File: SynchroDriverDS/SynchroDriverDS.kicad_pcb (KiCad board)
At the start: 2 copper layers, 67 x 33 mm, 46 parts, among them J1 POWER, J2 CTRL, J3 Conn_01x04, Q1 2N7002, Q2 2N7002, Q3 2N7002, Q4 SIS990, Q5 SIS990, Q6 SIS990, U1 DRV8300

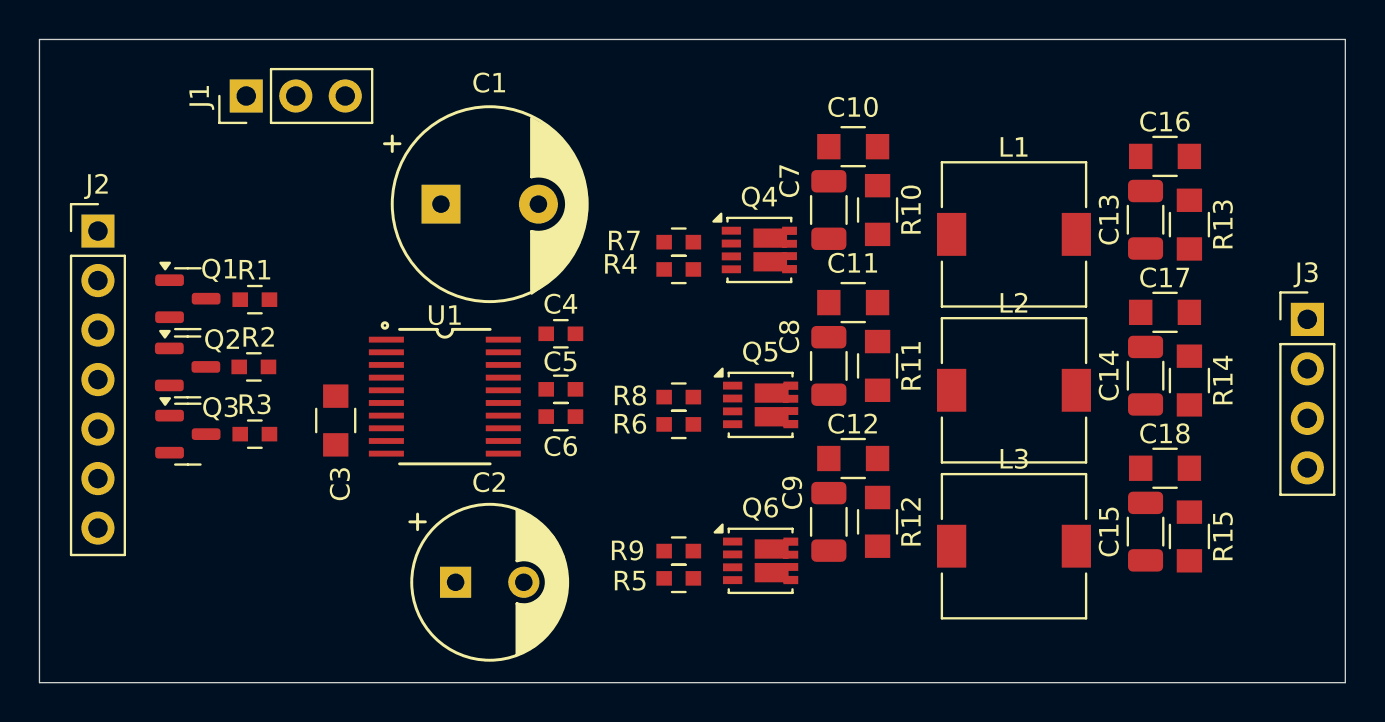
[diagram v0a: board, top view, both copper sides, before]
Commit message: Update digital single synchro pcb
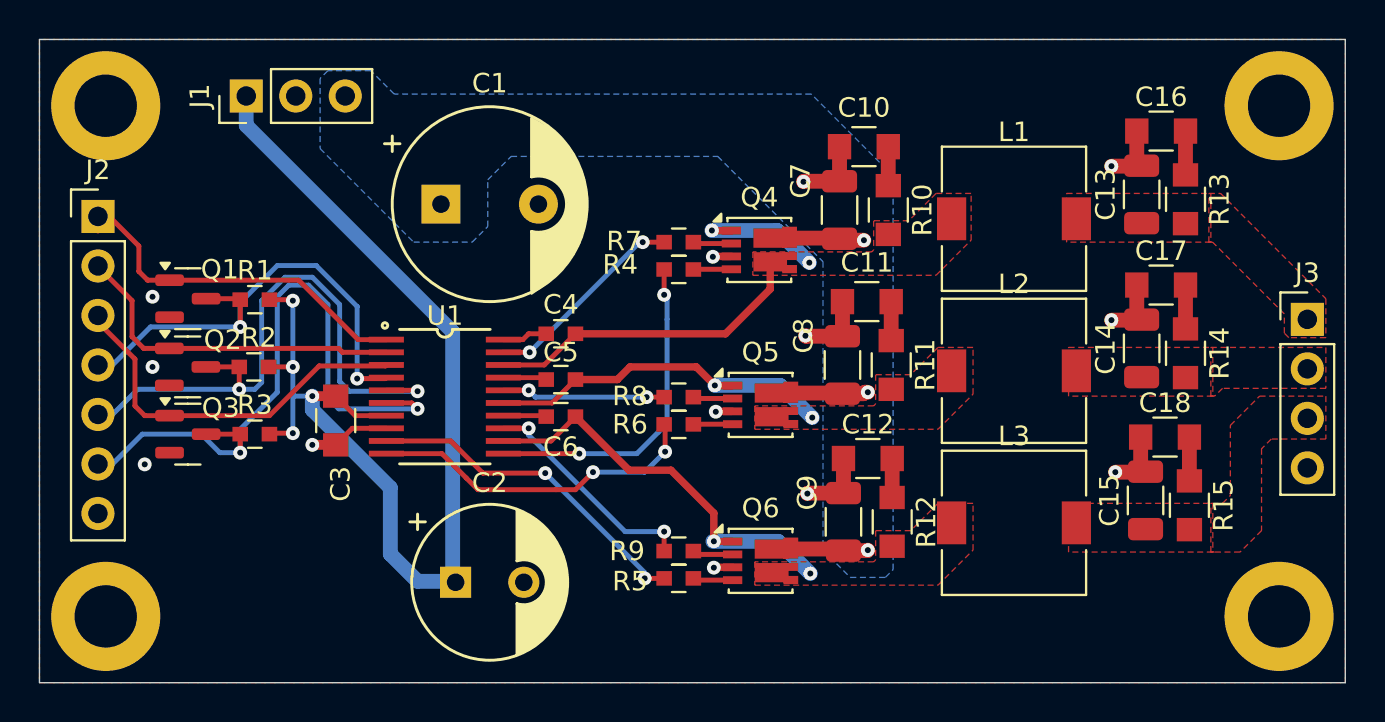
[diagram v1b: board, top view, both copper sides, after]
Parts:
- added H1: MountingHole_Pad, MountingHole:MountingHole_3.2mm_M3_DIN965_Pad, F.Cu at (123.4, 83.4)
- added H2: MountingHole_Pad, MountingHole:MountingHole_3.2mm_M3_DIN965_Pad, F.Cu at (123.4, 109.6)
- added H3: MountingHole_Pad, MountingHole:MountingHole_3.2mm_M3_DIN965_Pad, F.Cu at (183.6, 83.4)
- added H4: MountingHole_Pad, MountingHole:MountingHole_3.2mm_M3_DIN965_Pad, F.Cu at (183.6, 109.6)
- moved C15 1.60 mm to (176.8, 103.7)
- moved C18 1.60 mm to (177.8, 100.4)
- moved R15 1.60 mm to (179.0, 103.9)
- moved C14 1.41 mm to (176.6, 95.8)
- moved C17 1.41 mm to (177.6, 92.6)
- moved R14 1.41 mm to (178.8, 96.1)
- moved C13 1.32 mm to (176.6, 88.0)
- moved C16 1.32 mm to (177.6, 84.7)
- moved R13 1.32 mm to (178.8, 88.2)
- moved L3 1.20 mm to (170.0, 104.8)
- moved L2 1.00 mm to (170.0, 97.0)
- moved L1 0.80 mm to (170.0, 89.2)
- moved C12 0.75 mm to (162.5, 101.5)
- moved C9 0.75 mm to (161.2, 104.8)
- moved J2 0.75 mm to (123.0, 89.1)
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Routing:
- net +12V: track 0.00 -> 58.9 mm, vias 0 -> 4
- net /SingleSynchroDriver/INCL: track 0.00 -> 34.4 mm, vias 0 -> 2
- net /SingleSynchroDriver/INBL: track 0.00 -> 31.0 mm, vias 0 -> 2
- net GND: track 0.00 -> 28.2 mm, vias 0 -> 13
- net /SingleSynchroDriver/INAL: track 0.00 -> 25.4 mm, vias 0 -> 2
- net Net-(Q4A-S): track 0.00 -> 23.4 mm, vias 0 -> 2
- net Net-(Q6A-S): track 0.00 -> 21.5 mm, vias 0 -> 2
- net /SingleSynchroDriver/INC: track 0.00 -> 19.6 mm
- net Net-(Q5A-S): track 0.00 -> 18.6 mm, vias 0 -> 2
- net /SingleSynchroDriver/INA: track 0.00 -> 18.4 mm
- net /SingleSynchroDriver/INB: track 0.00 -> 17.7 mm
- net Net-(U1-GLC): track 0.00 -> 17.3 mm, vias 0 -> 2
- net Net-(U1-GLB): track 0.00 -> 17.3 mm, vias 0 -> 2
- net Net-(U1-GLA): track 0.00 -> 17.0 mm, vias 0 -> 2
- net +36V: track 0.00 -> 14.8 mm, vias 0 -> 3
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- added copper zone on B.Cu, net +36V
- added copper zone on F.Cu, net /SingleSynchroDriver/PHASE_A_OUT
- added copper zone on F.Cu, net /SingleSynchroDriver/PHASE_B_OUT
- added copper zone on F.Cu, net /SingleSynchroDriver/PHASE_C_OUT
- added copper zone on B.Cu, net GND
- added copper zone on F.Cu, net GND
- added copper zone on F.Cu, net Net-(Q4A-S)
- added copper zone on F.Cu, net Net-(Q5A-S)
- added copper zone on F.Cu, net Net-(Q6A-S)

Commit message: Improve ref in, clearance for 115V
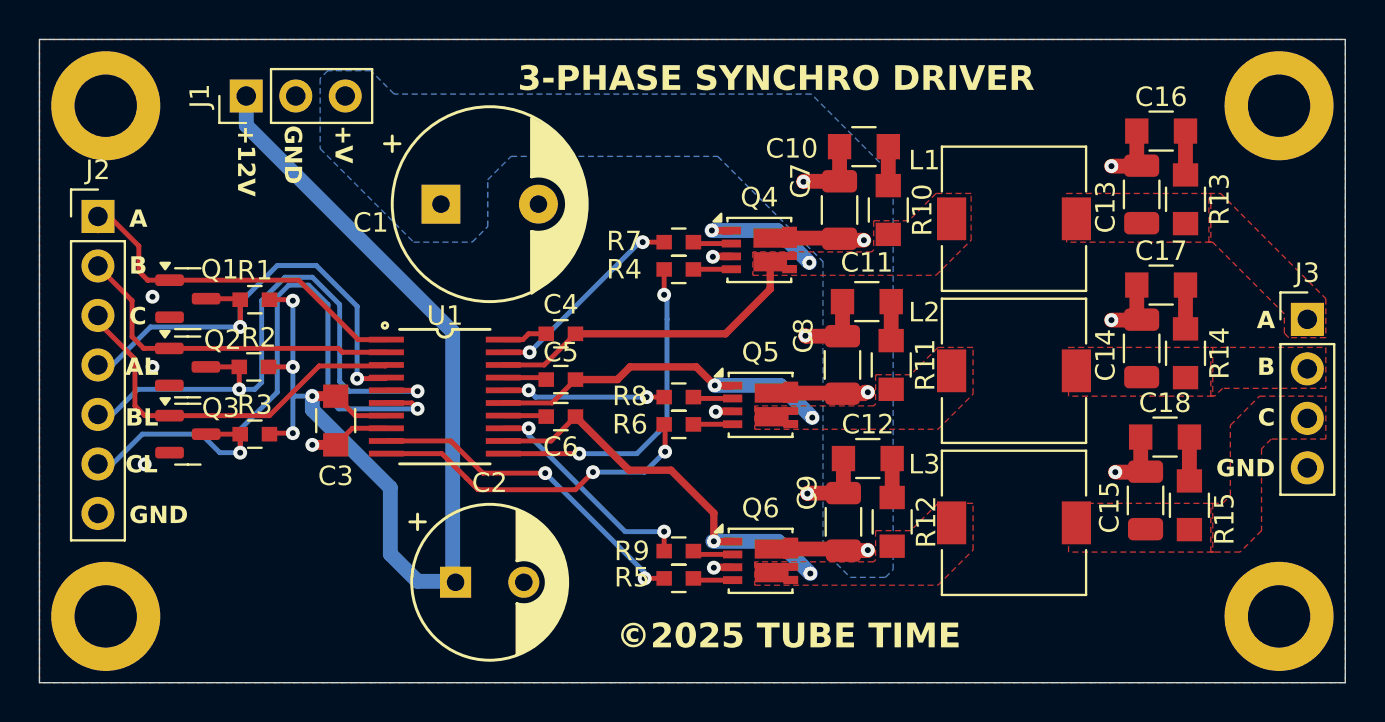
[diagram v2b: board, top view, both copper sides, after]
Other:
- board text added: "+12V"
- board text added: "+V"
- board text added: "3-PHASE SYNCHRO DRIVER"
- board text added: "A"
- board text added: "AL"
- board text added: "B"
- board text added: "BL"
- board text added: "C"
- board text added: "CL"
- board text added: "GND"
- board text added: "©2025 TUBE TIME"
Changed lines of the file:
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@@
 		(tags "resistor 0805")
 		(property "Reference" "C10"
-			(at 0 2 0)
+			(at 3.7 -0.1 0)
 			(layer "F.SilkS")
 			(effects
@@
 		(tags "Choke SMD")
 		(property "Reference" "L1"
-			(at 0 -4.45 0)
+			(at -4.6 -3 0)
 			(layer "F.SilkS")
 			(effects
@@
 		(tags "capacitor 0603")
 		(property "Reference" "R4"
-			(at -3 -0.25 0)
+			(at -2.8 0 0)
 			(layer "F.SilkS")
 			(effects
@@
 		(tags "capacitor")
 		(property "Reference" "C15"
-			(at 0 -1.85 90)
+			(at -0.35 -1.85 90)
 			(layer "F.SilkS")
 			(effects
@@
 		(tags "resistor 0805")
 		(property "Reference" "R15"
-			(at 0 1.75 90)
+			(at -0.7 1.8 90)
 			(layer "F.SilkS")
 			(effects
@@
 		(tags "Choke SMD")
 		(property "Reference" "L2"
-			(at 0 -4.45 0)
+			(at -4.6 -3 0)
 			(layer "F.SilkS")
 			(effects
@@
 		(tags "capacitor")
 		(property "Reference" "C13"
-			(at 0 -1.85 90)
+			(at -0.65 -1.85 90)
 			(layer "F.SilkS")
 			(effects
@@
 		(tags "resistor 0805")
 		(property "Reference" "C3"
-			(at 3.25 -0.25 90)
+			(at 2.85 0 180)
 			(layer "F.SilkS")
 			(effects
@@
 		(at 143.1 88.45)
 		(property "Reference" "C1"
-			(at 0 -6.2 0)
+			(at -6.1 0.95 0)
 			(layer "F.SilkS")
 			(effects
@@
 		(tags "capacitor")
 		(property "Reference" "C14"
-			(at 0 -1.85 90)
+			(at -0.35 -1.85 90)
 			(layer "F.SilkS")
 			(effects
@@
 		(tags "Choke SMD")
 		(property "Reference" "L3"
-			(at 0 -4.45 0)
+			(at -4.6 -3 0)
 			(layer "F.SilkS")
 			(effects
@@
 		(tags "capacitor 0603")
 		(property "Reference" "R5"
-			(at -2.5 0.15 0)
+			(at -2.4 -0.05 0)
 			(layer "F.SilkS")
 			(effects
@@
 		(tags "capacitor 0603")
 		(property "Reference" "R9"
-			(at -2.65 0 0)
+			(at -2.4 0 0)
 			(layer "F.SilkS")
 			(effects
@@
 		(layer "Edge.Cuts")
 	)
+	(gr_text "GND"
+		(at 133 84.4 270)
+		(layer "F.SilkS")
+		(effects
+			(font
+				(size 0.889 0.889)
+				(thickness 0.1524)
+				(bold yes)
+			)
+			(justify left)
+		)
+	)
+	(gr_text "B"
+		(at 183.4 96.8 0)
+		(layer "F.SilkS")
+		(effects
+			(font
+				(size 0.889 0.889)
+				(thickness 0.1524)
+				(bold yes)
+			)
+			(justify right)
+		)
+	)
+	(gr_text "BL"
+		(at 124.4 99.4 0)
+		(layer "F.SilkS")
+		(effects
+			(font
+				(size 0.889 0.889)
+				(thickness 0.1524)
+				(bold yes)
+			)
+			(justify left)
+		)
+	)
+	(gr_text "+12V"
+		(at 130.6 84.4 270)
+		(layer "F.SilkS")
+		(effects
+			(font
+				(size 0.889 0.889)
+				(thickness 0.1524)
+				(bold yes)
+			)
+			(justify left)
+		)
+	)
+	(gr_text "B"
+		(at 124.6 91.6 0)
+		(layer "F.SilkS")
+		(effects
+			(font
+				(size 0.889 0.889)
+				(thickness 0.1524)
+				(bold yes)
+			)
+			(justify left)
+		)
+	)
+	(gr_text "A"
+		(at 183.4 94.4 0)
+		(layer "F.SilkS")
+		(effects
+			(font
+				(size 0.889 0.889)
+				(thickness 0.1524)
+				(bold yes)
+			)
+			(justify right)
+		)
+	)
+	(gr_text "AL"
+		(at 124.4 96.8 0)
+		(layer "F.SilkS")
+		(effects
+			(font
+				(size 0.889 0.889)
+				(thickness 0.1524)
+				(bold yes)
+			)
+			(justify left)
+		)
+	)
+	(gr_text "CL"
+		(at 124.4 101.8 0)
+		(layer "F.SilkS")
+		(effects
+			(font
+				(size 0.889 0.889)
+				(thickness 0.1524)
+				(bold yes)
+			)
+			(justify left)
+		)
+	)
+	(gr_text "C"
+		(at 124.6 94.2 0)
+		(layer "F.SilkS")
+		(effects
+			(font
+				(size 0.889 0.889)
+				(thickness 0.1524)
+				(bold yes)
+			)
+			(justify left)
+		)
+	)
+	(gr_text "A"
+		(at 124.6 89.2 0)
+		(layer "F.SilkS")
+		(effects
+			(font
+				(size 0.889 0.889)
+				(thickness 0.1524)
+				(bold yes)
+			)
+			(justify left)
+		)
+	)
+	(gr_text "C"
+		(at 183.4 99.4 0)
+		(layer "F.SilkS")
+		(effects
+			(font
+				(size 0.889 0.889)
+				(thickness 0.1524)
+				(bold yes)
+			)
+			(justify right)
+		)
+	)
+	(gr_text "GND"
+		(at 183.4 102 0)
+		(layer "F.SilkS")
+		(effects
+			(font
+				(size 0.889 0.889)
+				(thickness 0.1524)
+				(bold yes)
+			)
+			(justify right)
+		)
+	)
+	(gr_text "3-PHASE SYNCHRO DRIVER"
+		(at 157.8 82 0)
+		(layer "F.SilkS")
+		(effects
+			(font
+				(size 1.27 1.27)
+				(thickness 0.1524)
+				(bold yes)
+			)
+		)
+	)
+	(gr_text "©2025 TUBE TIME"
+		(at 149.6 110.6 0)
+		(layer "F.SilkS")
+		(effects
+			(font
+				(size 1.27 1.27)
+				(thickness 0.1524)
+				(bold yes)
+			)
+			(justify left)
+		)
+	)
+	(gr_text "GND"
+		(at 124.6 104.4 0)
+		(layer "F.SilkS")
+		(effects
+			(font
+				(size 0.889 0.889)
+				(thickness 0.1524)
+				(bold yes)
+			)
+			(justify left)
+		)
+	)
+	(gr_text "+V"
+		(at 135.6 84.4 270)
+		(layer "F.SilkS")
+		(effects
+			(font
+				(size 0.889 0.889)
+				(thickness 0.1524)
+				(bold yes)
+			)
+			(justify left)
+		)
+	)
 	(segment
